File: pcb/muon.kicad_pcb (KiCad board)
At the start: 2 copper layers, 72 x 59 mm, 57 parts, among them J1 Debug Pins, J2 USB_C_Receptacle_USB2.0, SW1 Kailh Hotswap, SW2 Kailh Hotswap, SW3 Reset, SW7 Kailh Hotswap, U1 SRV05-4, U2 TLV75533PDBVR, U3 RP2040, U4 W25Q80DVSSIG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

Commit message: broad strokes
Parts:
- added ?: , , F.Cu at (122.5, 60.0)
- added ?: , , F.Cu at (122.5, 105.0)
- added ?: , , F.Cu at (184.5, 105.0)
- added REF**: MountingHole_2.5mm_Pad, MountingHole:MountingHole_2.5mm_Pad, F.Cu at (184.5, 60.0)
- moved U1 1.55 mm to (152.8, 61.5)
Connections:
- U1 pad 3: /D- -> /D+
- U1 pad 4: /D+ -> /D-
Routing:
- net /D-: track 30.1 -> 27.3 mm
- net /D+: track 29.8 -> 27.8 mm
- net GND: track 21.6 -> 23.0 mm
- net /VBUS_: track 21.6 -> 22.9 mm

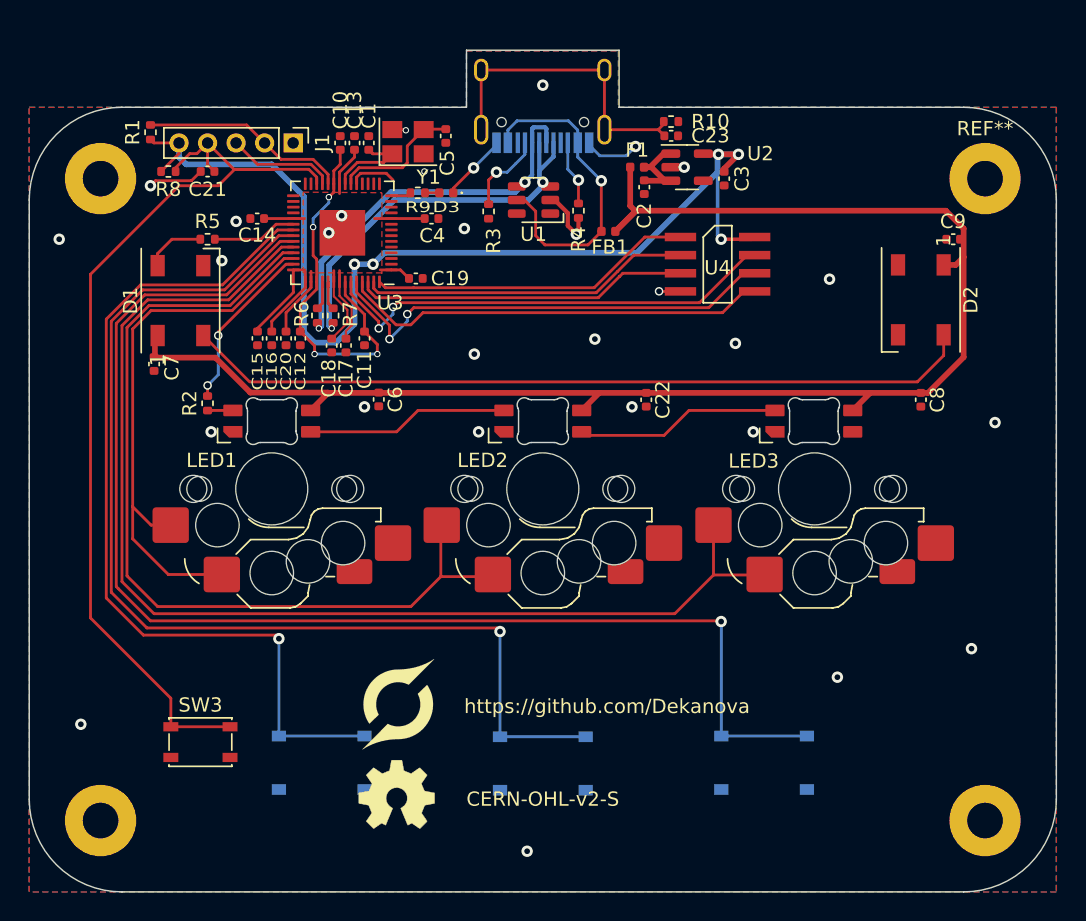
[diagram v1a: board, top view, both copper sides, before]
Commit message: usb back on main side
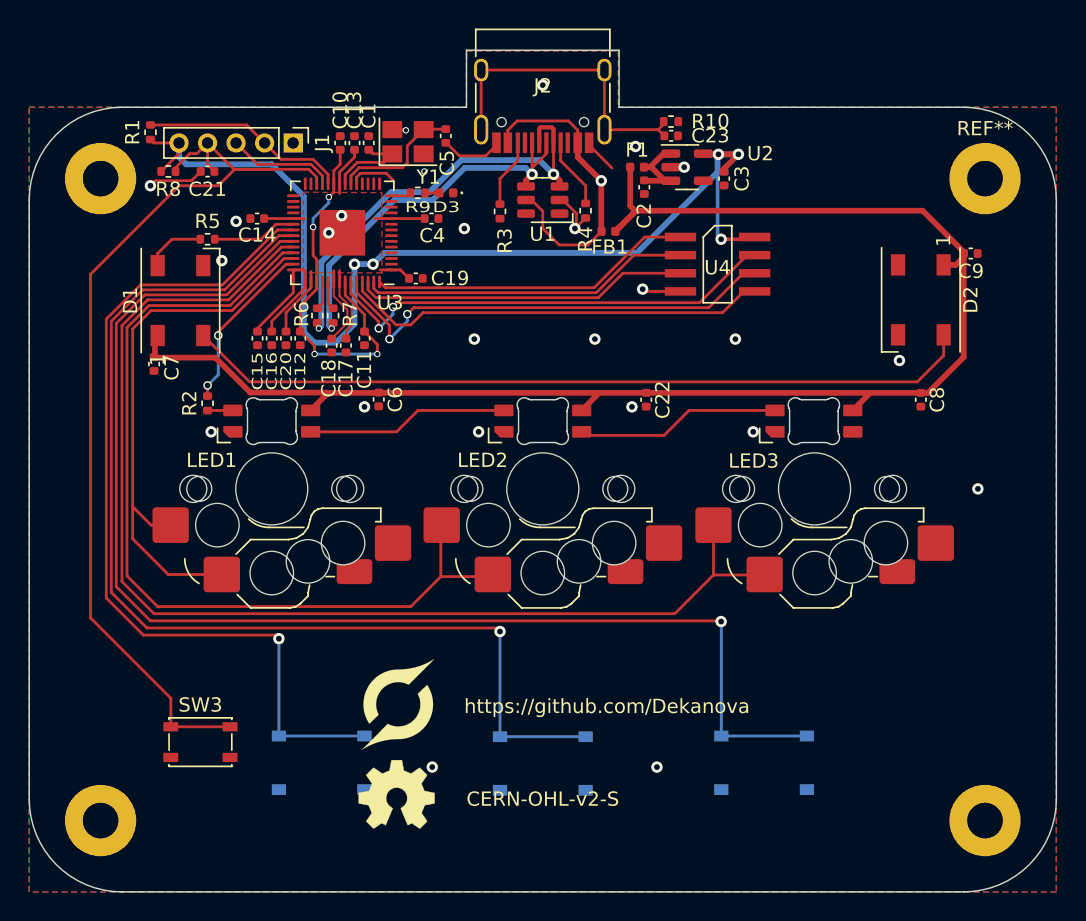
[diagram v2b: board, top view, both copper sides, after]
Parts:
- J2: moved to F.Cu
- moved C9 1.59 mm to (183.5, 65.2), turned to 0 degrees
- moved R3 0.80 mm to (150.5, 62.3)
- moved kibuzzard-63119D27 0.75 mm to (178.0, 59.5)
- moved kibuzzard-63119D36 0.75 mm to (172.2, 59.5)
- moved U1 0.65 mm to (153.5, 61.5)
- moved R4 0.50 mm to (156.5, 62.2)
- turned J2 to 180 degrees
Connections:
- R3 pad 2: Net-(J2-PadA5) -> Net-(J2-PadB5)
- R4 pad 2: Net-(J2-PadB5) -> Net-(J2-PadA5)
- U1 pad 3: /D+ -> /D-
- U1 pad 4: /D- -> /D+
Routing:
- net /D-: track 27.3 -> 30.7 mm
- net GND: track 23.0 -> 21.0 mm, vias 29 -> 25
- net /5V_LED: track 107.0 -> 106.1 mm
- net /VBUS_: track 22.9 -> 21.9 mm
- net Net-(J2-PadA5): track 5.80 -> 4.98 mm, vias 1 -> 0
- net Net-(J2-PadB5): track 4.57 -> 4.82 mm, vias 1 -> 0

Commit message: final touches & export fab files
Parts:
- moved C9 0.10 mm to (183.6, 65.2)
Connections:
- ? pad 1: (no net) -> GND (x3)
- REF** pad 1: (no net) -> GND
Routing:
- net +3V3: track 115.2 -> 111.7 mm, vias 5 -> 3

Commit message: release v0.5
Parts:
- removed kibuzzard-63119D27: G***, kibuzzard-63119D27
- removed kibuzzard-63119D36: G***, kibuzzard-63119D36
- added kibuzzard-6355061C: G***, kibuzzard-6355061C, B.Cu at (171.7, 59.5)
- added kibuzzard-6355064D: G***, kibuzzard-6355064D, B.Cu at (177.2, 59.5)

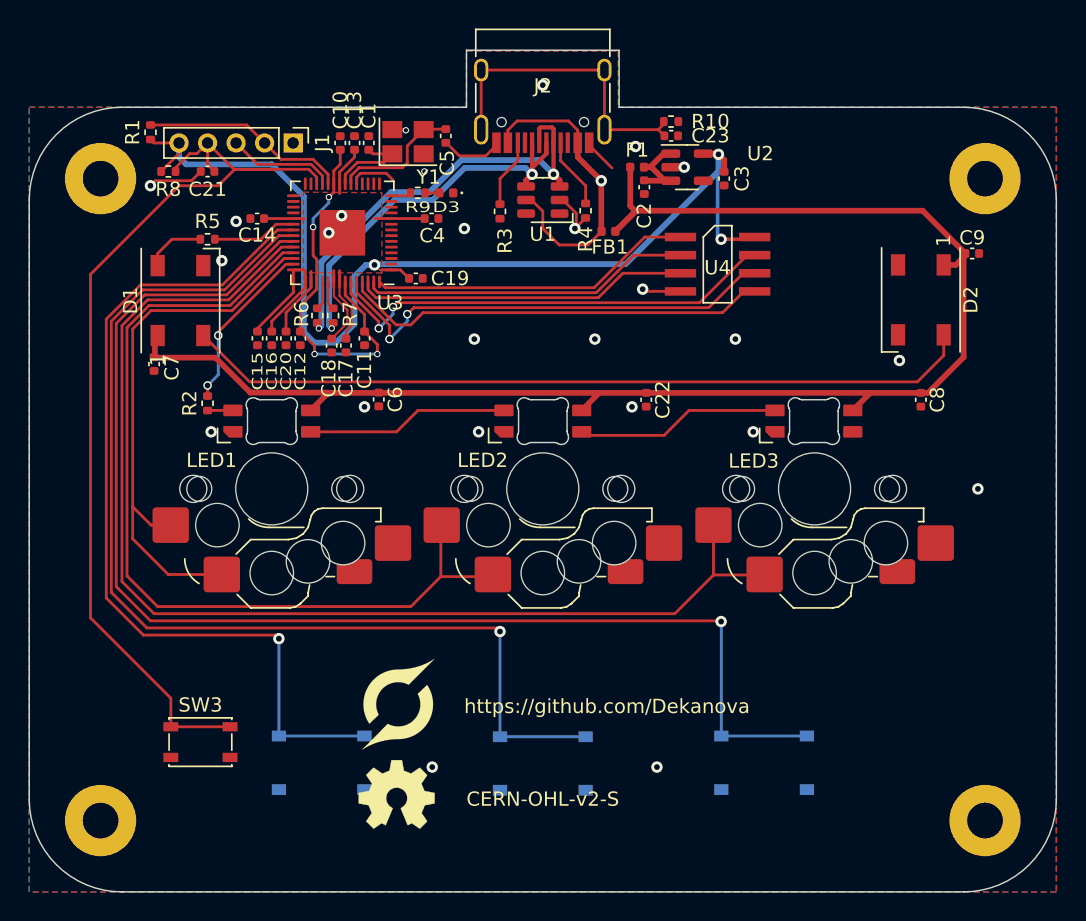
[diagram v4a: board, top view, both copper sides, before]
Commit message: Pre-v0.6 - use TagConnect debug header - equally space underglow LEDs - add comment to replicate kibuzzard settings - use M3 mounting holes
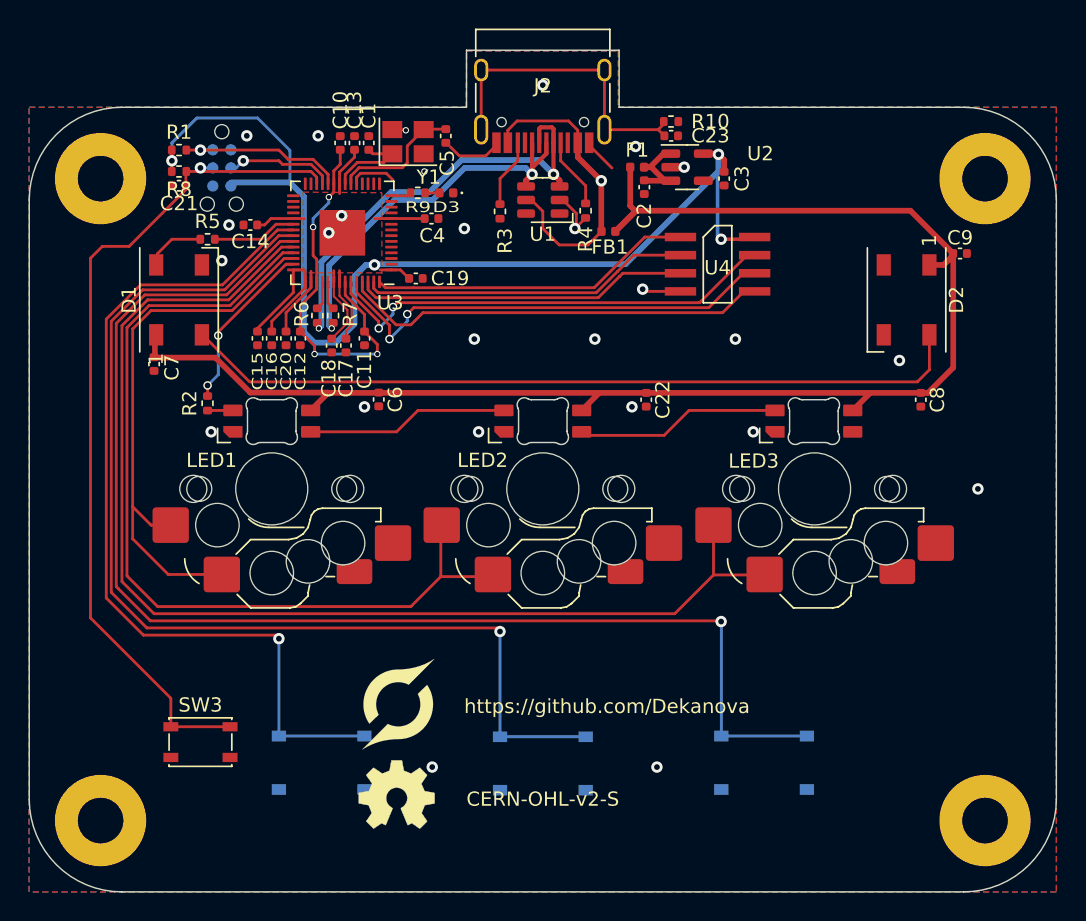
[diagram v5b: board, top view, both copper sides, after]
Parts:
- removed REF**: MountingHole_2.5mm_Pad, MountingHole:MountingHole_2.5mm_Pad
- removed kibuzzard-6355061C: G***, kibuzzard-6355061C
- removed kibuzzard-6355064D: G***, kibuzzard-6355064D
- added ?: , , F.Cu at (184.5, 60.0)
- added kibuzzard-63718431: G***, kibuzzard-63718431, B.Cu at (171.8, 59.2)
- added kibuzzard-63718440: G***, kibuzzard-63718440, B.Cu at (176.8, 59.2)
- J1: footprint Connector_PinHeader_2.00mm:PinHeader_1x05_P2.00mm_Vertical -> Connector:Tag-Connect_TC2030-IDC-NL_2x03_P1.27mm_Vertical; moved to B.Cu
- moved J1 5.30 mm to (131.0, 59.2)
- moved R1 2.36 mm to (128.0, 58.0), turned to 0 degrees
- moved C21 2.24 mm to (128.0, 60.5)
- moved D2 1.00 mm to (179.0, 68.5)
- moved C9 0.85 mm to (182.8, 65.2)
- moved R8 0.75 mm to (128.0, 59.5)
- moved C14 0.66 mm to (133.0, 63.2)
- moved D1 0.11 mm to (128.0, 68.5)
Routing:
- net /~{RESET}: track 68.6 -> 60.1 mm, vias 0 -> 1
- net +3V3: track 111.7 -> 117.4 mm, vias 3 -> 4
- net GND: track 21.0 -> 17.0 mm, vias 25 -> 26
- net /SWCLK: track 14.5 -> 12.2 mm, vias 0 -> 1
- net /5V_LED: track 106.1 -> 105.3 mm
- net /SWD: track 7.57 -> 7.62 mm, vias 0 -> 1
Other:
- board text added: "Kibuzzard Settings: - RobotoMono-B - / caps - 1mm height - Align Left"
- board text removed: "3v3"
- board text removed: "CLK"
- board text removed: "GND"
- board text removed: "RST"
- board text removed: "SWD"

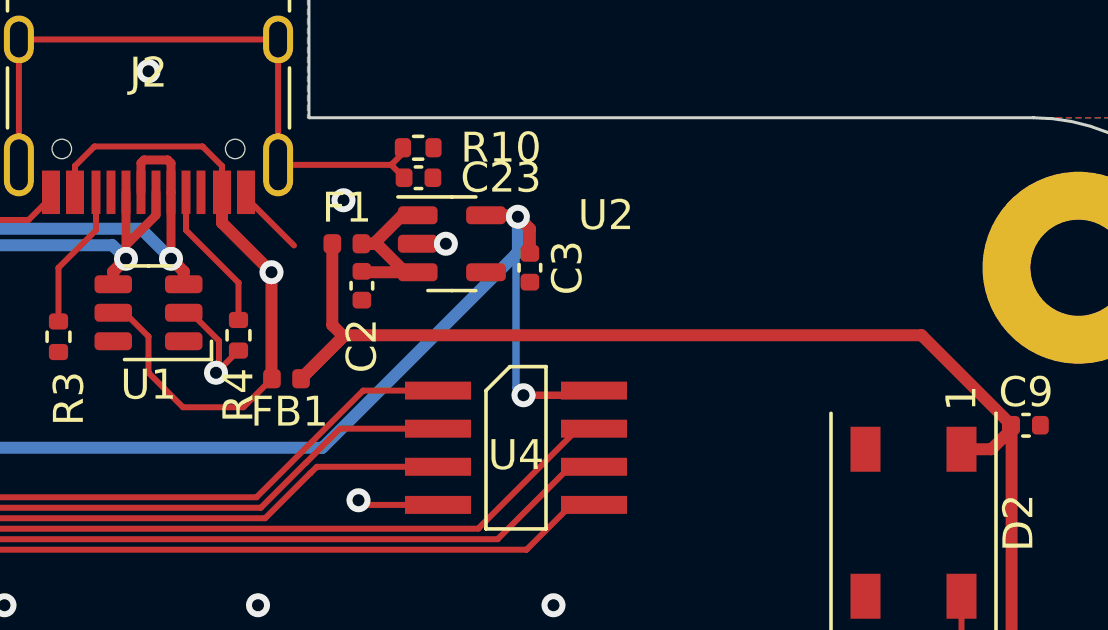
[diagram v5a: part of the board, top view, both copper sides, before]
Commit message: update page titles, use an actual Ferrite Bead (has just been a 0ohm resistor till now
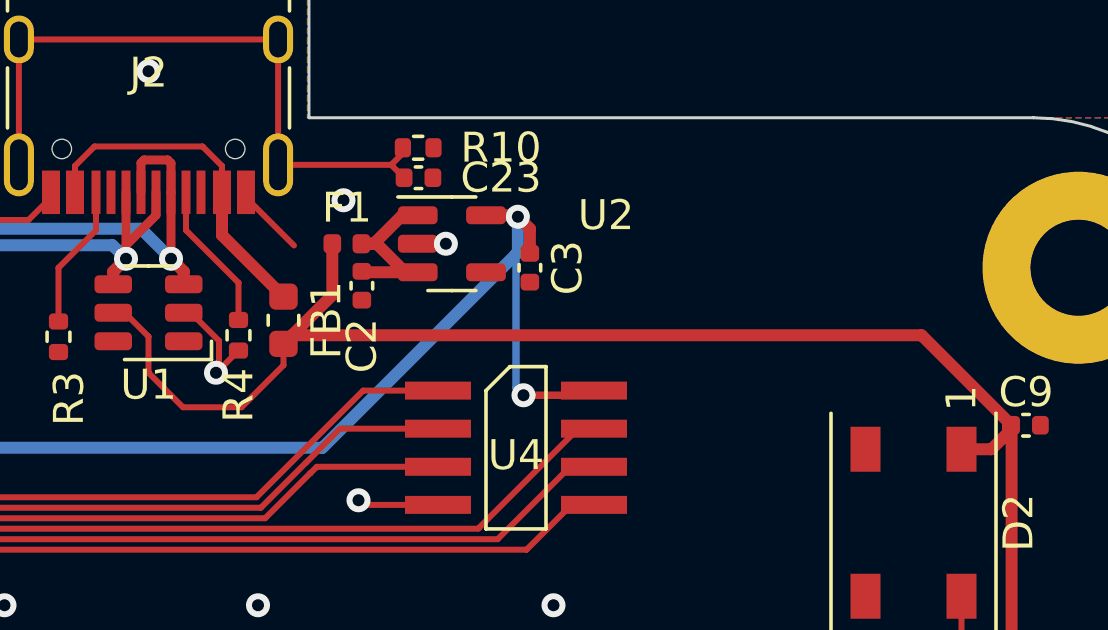
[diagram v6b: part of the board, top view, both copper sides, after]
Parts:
- FB1: value ~ -> BLM18HE152SN1D; footprint Inductor_SMD:L_0402_1005Metric -> Inductor_SMD:L_0603_1608Metric
- moved FB1 1.95 mm to (158.0, 61.8), turned to -90 degrees
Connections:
- U1 pad 5: /VBUS_ -> /5V_LED
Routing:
- net /VBUS_: track 21.9 -> 11.5 mm, vias 1 -> 0
- net /5V_LED: track 105.3 -> 113.3 mm
